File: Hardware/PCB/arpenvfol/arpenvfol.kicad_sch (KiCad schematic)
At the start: 74 parts, among them J1 Synth_power_2x5, J10 3_pin_Molex_header, J2 AudioJack2_SwitchT, J3 AudioJack2_SwitchT, J4 AudioJack2_SwitchT, J5 AudioJack2, J6 AudioJack2, J7 2_pin_Molex_connector, J8 2_pin_Molex_header, J9 3_pin_Molex_connector, Q1 2N3904, Q2 2N3904, U1 TL074

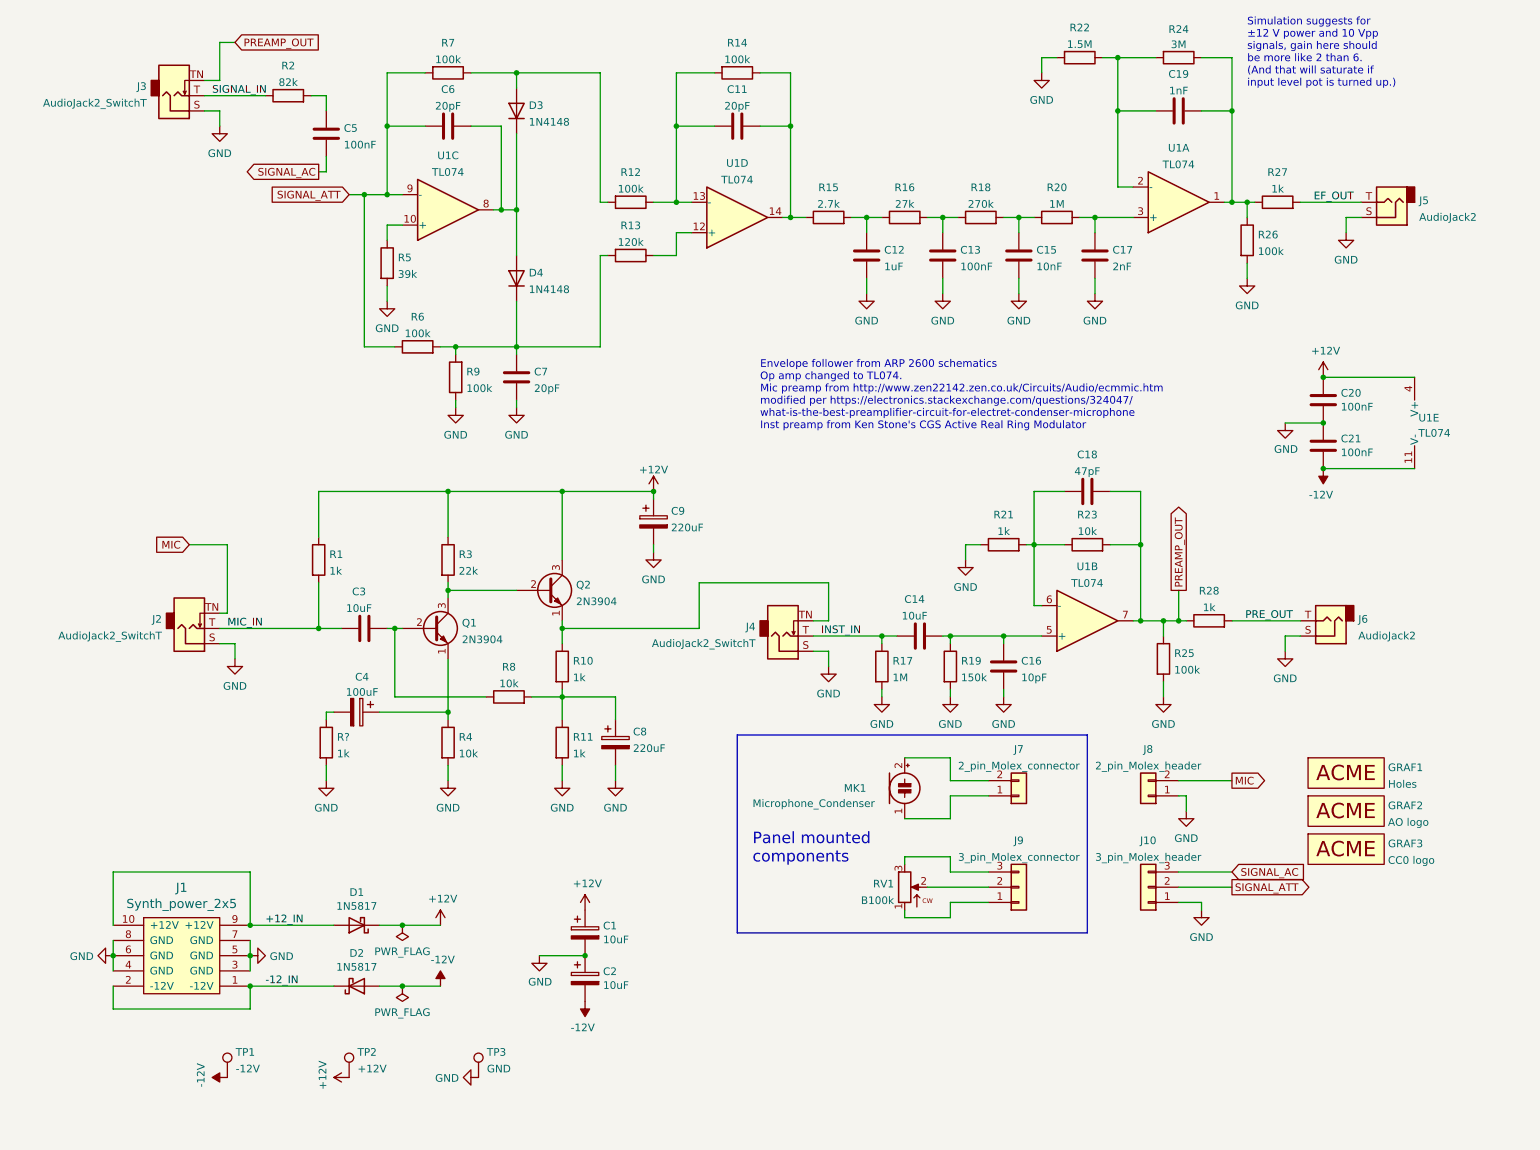
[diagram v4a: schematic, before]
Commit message: Change transistor, annotate, LTSpice simulation
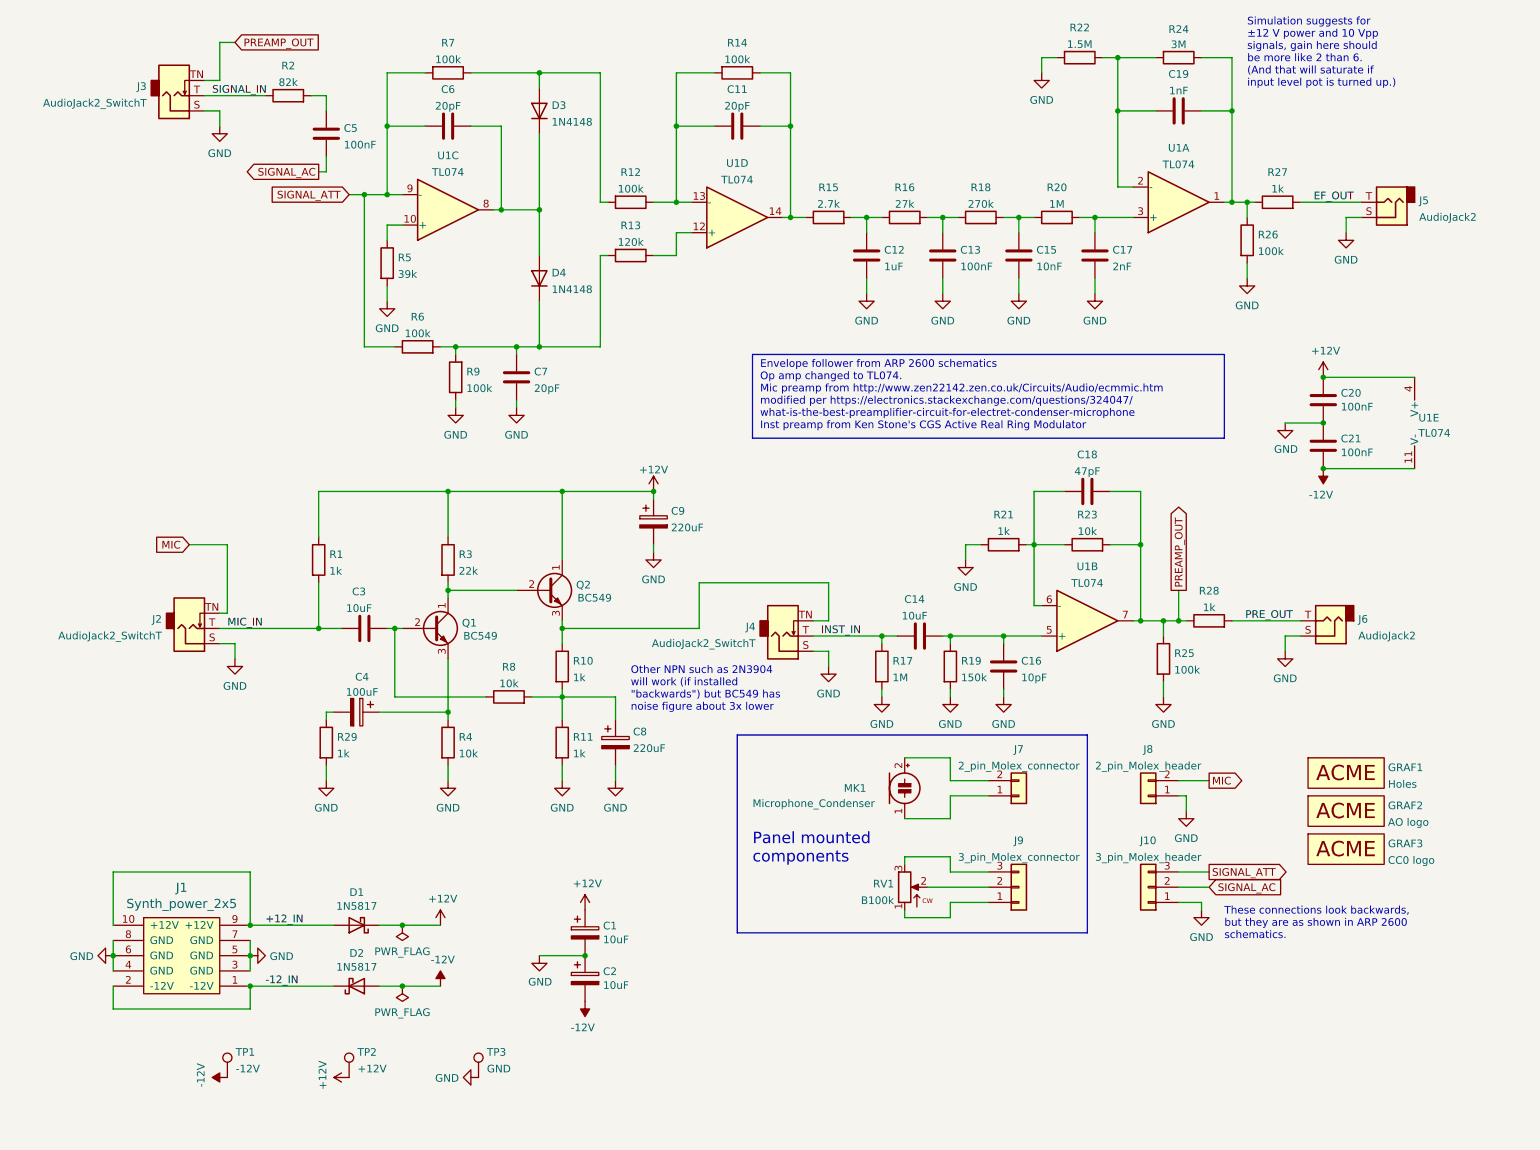
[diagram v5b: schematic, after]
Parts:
- C12: footprint ao_tht:C_Rect_L7.2mm_W2.5mm_P5.00mm_FKS2_FKP2_MKS2_MKP2 -> ao_tht:C_Rect_L7.2mm_W7.2mm_P5.00mm_FKS2_FKP2_MKS2_MKP2
- Q1, Q2: value 2N3904 -> BC549; symbol ao_symbols:2N3904 -> Transistor_BJT:BC549
- gave numbers to parts that had none: 1
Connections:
- net +12V: now also Q2.1 (C); no longer Q2.3 (C)
- net SIGNAL_AC: now also J10.2 (Pin_2); no longer J10.3 (Pin_3)
- net SIGNAL_ATT: now also J10.3 (Pin_3); no longer J10.2 (Pin_2)
- net at C4.1, R4.1: now also Q1.3 (E); no longer Q1.1 (E)
- net at Q2.2 (B), R3.2: now also Q1.1 (C); no longer Q1.3 (C)
- net at J4.TN, R10.1: now also Q2.3 (E); no longer Q2.1 (E)
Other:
- note added: "Other NPN such as 2N3904 will work (if installed "backwards") but BC549 has noise figure about 3x lower"
- note added: "These connections look backwards, but they are as shown in ARP 2600 schematics."
- moved on the sheet: D3, D4

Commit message: Panel; add gain pot
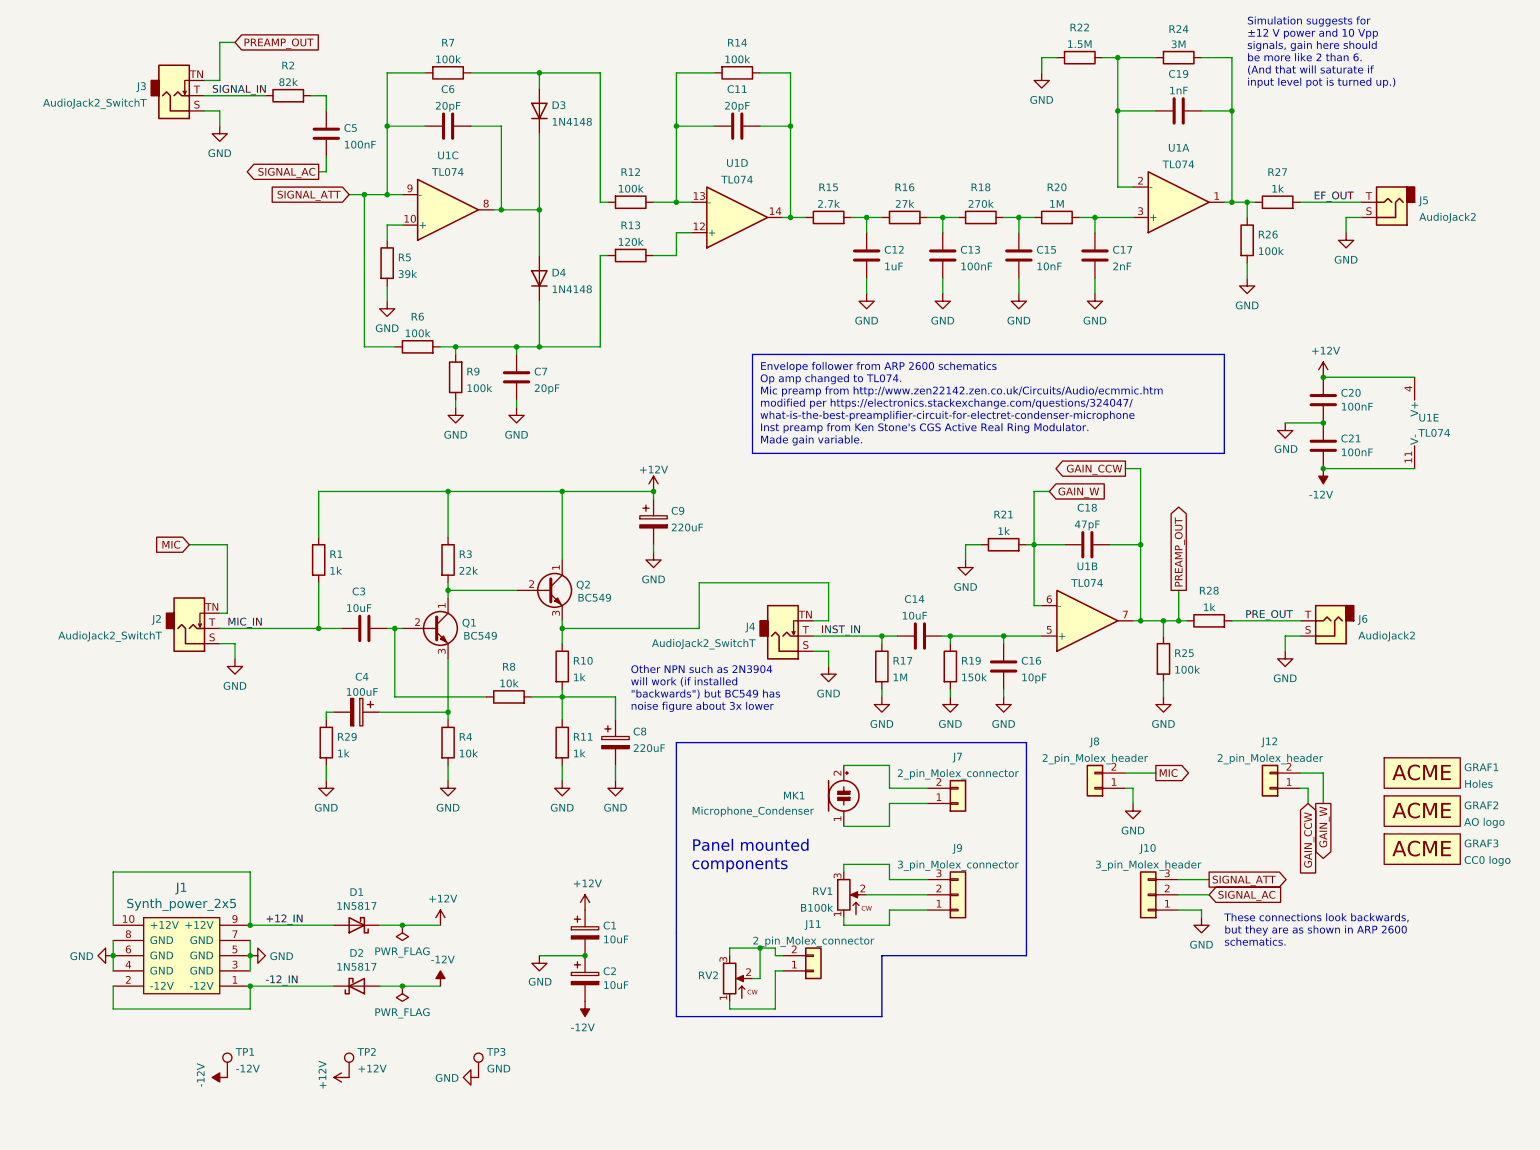
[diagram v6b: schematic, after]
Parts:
- removed R23: 10k, ao_tht:R_Axial_DIN0207_L6.3mm_D2.5mm_P10.16mm_Horizontal, symbol ao_symbols:R
- added J11: 2_pin_Molex_connector, ao_tht:Molex_KK-254_AE-6410-02A_1x02_P2.54mm_Vertical, symbol ao_symbols:2_pin_Molex_connector
- added J12: 2_pin_Molex_header, ao_tht:Molex_KK-254_AE-6410-02A_1x02_P2.54mm_Vertical, symbol ao_symbols:2_pin_Molex_header
- added RV2: (no value), symbol ao_symbols:R_POT
- C11, C16, C18, C6, C7: footprint ao_tht:C_Disc_D3.0mm_W1.6mm_P2.50mm -> (none)
- C12: footprint ao_tht:C_Rect_L7.2mm_W7.2mm_P5.00mm_FKS2_FKP2_MKS2_MKP2 -> (none)
- C13, C15, C17, C19, C5: footprint ao_tht:C_Rect_L7.2mm_W2.5mm_P5.00mm_FKS2_FKP2_MKS2_MKP2 -> (none)
- C14, C3: footprint ao_tht:C_Radial_D8.0mm_H11.5mm_P3.50mm -> (none)
- J7: footprint (none) -> ao_tht:Molex_KK-254_AE-6410-02A_1x02_P2.54mm_Vertical
- J9: footprint (none) -> ao_tht:Molex_KK-254_AE-6410-03A_1x03_P2.54mm_Vertical
- Q1, Q2: footprint ao_tht:TO-92_Inline_Wide -> (none)
- TP1, TP2: Config (none) -> DNF
- TP3: footprint ao_tht:TestPoint_THTPad_1.5x1.5mm_Drill0.7mm -> (none); Config (none) -> DNF
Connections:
- net GAIN_W: now reaches C18.1, R21.2, U1.6 (-)
- net GAIN_W: now also J12.2 (Pin_2)
- net PREAMP_OUT renamed GAIN_CCW
- net GAIN_CCW: now also J12.1 (Pin_1)
- new net: J11.1 (Pin_1), RV2.1
- new net: J11.2 (Pin_2), RV2.2, RV2.3
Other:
- note added: "Envelope follower from ARP 2600 schematics Op amp changed to TL074. Mic preamp from http://www.zen22142.zen.co.uk/Circuits/Audio/ecmmic.htm modified per https://electronics.stackexchange.com/questions/324047/ what-is-the-best-preamplifier-circuit-for-electret-condenser-microphone Inst preamp from Ken Stone's CGS Active Real Ring Modulator. Made gain variable."
- note removed: "Envelope follower from ARP 2600 schematics Op amp changed to TL074. Mic preamp from http://www.zen22142.zen.co.uk/Circuits/Audio/ecmmic.htm modified per https://electronics.stackexchange.com/questions/324047/ what-is-the-best-preamplifier-circuit-for-electret-condenser-microphone Inst preamp from Ken Stone's CGS Active Real Ring Modulator"
- moved on the sheet: C18, GRAF1, GRAF2, GRAF3, J10, J7, J8, J9, MK1, RV1

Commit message: Schem reorg
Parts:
- C11, C16, C18, C6, C7: footprint (none) -> ao_tht:C_Disc_D5.0mm_W2.5mm_P5.00mm
- C12: footprint (none) -> ao_tht:C_Rect_L7.2mm_W7.2mm_P5.00mm_FKS2_FKP2_MKS2_MKP2
- C13, C15, C17, C19, C5: footprint (none) -> ao_tht:C_Rect_L7.2mm_W2.5mm_P5.00mm_FKS2_FKP2_MKS2_MKP2
- C14, C3: footprint (none) -> ao_tht:C_Radial_D8.0mm_H11.5mm_P3.50mm
- Q1, Q2: footprint (none) -> ao_tht:TO-92_Inline_Wide
- RV2: value (none) -> B10k
- TP3: footprint (none) -> ao_tht:TestPoint_THTPad_1.5x1.5mm_Drill0.7mm
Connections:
- net MIC_OUT: now reaches J4.TN, Q2.3 (E), R10.1
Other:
- note added: "Follower"
- note added: "For ±12 V power and 10 Vpp signals, gain here should be more like 2 than 6. (And that will saturate if input level pot is turned up.)"
- note added: "Instrument preamp"
- note added: "Mic preamp"
- note added: "Power"
- note removed: "Simulation suggests for ±12 V power and 10 Vpp signals, gain here should be more like 2 than 6. (And that will saturate if input level pot is turned up.)"
- moved on the sheet: C1, C11, C12, C13, C14, C15, C16, C17, C18, C2, C20, C21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

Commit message: Final pre fab tweaks, Gerbers, schematic, BOM
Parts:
- C1: renamed from C4; value 100uF -> (none); footprint ao_tht:CP_Radial_D6.3mm_P2.50mm -> (none); SKU (none) -> A-4538
- C10: renamed from C20; value 100nF -> (none); footprint ao_tht:C_Disc_D3.0mm_W1.6mm_P2.50mm -> (none)
- C11: renamed from C21; value 100nF -> (none); footprint ao_tht:C_Disc_D3.0mm_W1.6mm_P2.50mm -> (none)
- C12: renamed from C11; value 20pF -> (none); footprint ao_tht:C_Disc_D5.0mm_W2.5mm_P5.00mm -> (none)
- C13: renamed from C12; value 1uF -> (none); footprint ao_tht:C_Rect_L7.2mm_W7.2mm_P5.00mm_FKS2_FKP2_MKS2_MKP2 -> (none); SKU (none) -> A-4168
- C14: renamed from C13; value 100nF -> (none); footprint ao_tht:C_Rect_L7.2mm_W2.5mm_P5.00mm_FKS2_FKP2_MKS2_MKP2 -> (none); SKU (none) -> A-564
- C15: renamed from C14; value 10uF -> (none); footprint ao_tht:C_Radial_D8.0mm_H11.5mm_P3.50mm -> (none); SKU A-4349 -> A-4216
- C16: renamed from C15; value 10nF -> (none); footprint ao_tht:C_Rect_L7.2mm_W2.5mm_P5.00mm_FKS2_FKP2_MKS2_MKP2 -> (none); SKU (none) -> A-559
- C17: renamed from C16; value 10pF -> (none); footprint ao_tht:C_Disc_D5.0mm_W2.5mm_P5.00mm -> (none)
- C18: renamed from C17; value 2nF -> (none); footprint ao_tht:C_Rect_L7.2mm_W2.5mm_P5.00mm_FKS2_FKP2_MKS2_MKP2 -> (none); SKU (none) -> A-558
- C19: renamed from C18; value 47pF -> (none); footprint ao_tht:C_Disc_D5.0mm_W2.5mm_P5.00mm -> (none)
- C2: renamed from C5; value 100nF -> (none); footprint ao_tht:C_Rect_L7.2mm_W2.5mm_P5.00mm_FKS2_FKP2_MKS2_MKP2 -> (none); SKU (none) -> A-564
- C20: renamed from C19; value 1nF -> (none); footprint ao_tht:C_Rect_L7.2mm_W2.5mm_P5.00mm_FKS2_FKP2_MKS2_MKP2 -> (none); SKU (none) -> A-1531, A-557
- C3: value 10uF -> (none); footprint ao_tht:C_Radial_D8.0mm_H11.5mm_P3.50mm -> (none); SKU A-4349 -> A-4216
- C4: renamed from C6; value 20pF -> (none); footprint ao_tht:C_Disc_D5.0mm_W2.5mm_P5.00mm -> (none)
- C5: renamed from C7; value 20pF -> (none); footprint ao_tht:C_Disc_D5.0mm_W2.5mm_P5.00mm -> (none)
- C6: renamed from C1; value 10uF -> (none); footprint ao_tht:CP_Radial_D6.3mm_P2.50mm -> (none)
- C7: renamed from C2; value 10uF -> (none); footprint ao_tht:CP_Radial_D6.3mm_P2.50mm -> (none)
- C8, C9: value 220uF -> (none); footprint ao_tht:CP_Radial_D6.3mm_P2.50mm -> (none); SKU (none) -> A-1064
- D1, D2: value 1N5817 -> (none); footprint ao_tht:D_DO-41_SOD81_P10.16mm_Horizontal -> (none)
- D3, D4: value 1N4148 -> (none); footprint ao_tht:D_DO-35_SOD27_P7.62mm_Horizontal -> (none)
- GRAF1: value Holes -> (none); footprint arpenvfol:arpenvfol_panel_holes -> (none)
- GRAF2: value AO logo -> (none); footprint ao_tht:analogoutput_12mm -> (none)
- GRAF3: value CC0 logo -> (none); footprint ao_tht:CC0_logo -> (none)
- J1: renamed from J2; value AudioJack2_SwitchT -> (none); footprint ao_tht:Jack_6.35mm_PJ_629HAN_slots -> (none)
- J10: value 3_pin_Molex_header -> (none); footprint ao_tht:Molex_KK-254_AE-6410-03A_1x03_P2.54mm_Vertical -> (none)
- J11: renamed from J5; value AudioJack2 -> (none); footprint ao_tht:Jack_6.35mm_PJ_629HAN_slots -> (none)
- J12: renamed from J6; value AudioJack2 -> (none); footprint ao_tht:Jack_6.35mm_PJ_629HAN_slots -> (none)
- J2: renamed from J3; value AudioJack2_SwitchT -> (none); footprint ao_tht:Jack_6.35mm_PJ_629HAN_slots -> (none)
- J3: renamed from J1; value Synth_power_2x5 -> (none); footprint ao_tht:Power_Header -> (none)
- J4: value AudioJack2_SwitchT -> (none); footprint ao_tht:Jack_6.35mm_PJ_629HAN_slots -> (none)
- J5: renamed from J7; value 2_pin_Molex_connector -> (none); footprint ao_tht:Molex_KK-254_AE-6410-02A_1x02_P2.54mm_Vertical -> (none)
- J6: renamed from J11; value 2_pin_Molex_connector -> (none); footprint ao_tht:Molex_KK-254_AE-6410-02A_1x02_P2.54mm_Vertical -> (none)
- J7: renamed from J9; value 3_pin_Molex_connector -> (none); footprint ao_tht:Molex_KK-254_AE-6410-03A_1x03_P2.54mm_Vertical -> (none)
- J8: value 2_pin_Molex_header -> (none); footprint ao_tht:Molex_KK-254_AE-6410-02A_1x02_P2.54mm_Vertical -> (none)
- J9: renamed from J12; value 2_pin_Molex_header -> (none); footprint ao_tht:Molex_KK-254_AE-6410-02A_1x02_P2.54mm_Vertical -> (none)
- MK1: value Microphone_Condenser -> (none)
- Q1, Q2: value BC549 -> (none); footprint ao_tht:TO-92_Inline_Wide -> (none)
- R1, R27, R28: value 1k -> (none); footprint ao_tht:R_Axial_DIN0207_L6.3mm_D2.5mm_P10.16mm_Horizontal -> (none)
- R10: renamed from R8; value 10k -> (none); footprint ao_tht:R_Axial_DIN0207_L6.3mm_D2.5mm_P10.16mm_Horizontal -> (none)
- R11: renamed from R10; value 1k -> (none); footprint ao_tht:R_Axial_DIN0207_L6.3mm_D2.5mm_P10.16mm_Horizontal -> (none)
- R12: renamed from R11; value 1k -> (none); footprint ao_tht:R_Axial_DIN0207_L6.3mm_D2.5mm_P10.16mm_Horizontal -> (none)
- R13: renamed from R12; value 100k -> (none); footprint ao_tht:R_Axial_DIN0207_L6.3mm_D2.5mm_P10.16mm_Horizontal -> (none)
- R14: renamed from R13; value 120k -> (none); footprint ao_tht:R_Axial_DIN0207_L6.3mm_D2.5mm_P10.16mm_Horizontal -> (none)
- R15: renamed from R14; value 100k -> (none); footprint ao_tht:R_Axial_DIN0207_L6.3mm_D2.5mm_P10.16mm_Horizontal -> (none)
- R16: renamed from R15; value 2.7k -> (none); footprint ao_tht:R_Axial_DIN0207_L6.3mm_D2.5mm_P10.16mm_Horizontal -> (none)
- R17: renamed from R16; value 27k -> (none); footprint ao_tht:R_Axial_DIN0207_L6.3mm_D2.5mm_P10.16mm_Horizontal -> (none)
- R18: renamed from R17; value 1M -> (none); footprint ao_tht:R_Axial_DIN0207_L6.3mm_D2.5mm_P10.16mm_Horizontal -> (none)
- R19: renamed from R18; value 270k -> (none); footprint ao_tht:R_Axial_DIN0207_L6.3mm_D2.5mm_P10.16mm_Horizontal -> (none)
- R2: value 82k -> (none); footprint ao_tht:R_Axial_DIN0207_L6.3mm_D2.5mm_P10.16mm_Horizontal -> (none)
- R20: renamed from R19; value 150k -> (none); footprint ao_tht:R_Axial_DIN0207_L6.3mm_D2.5mm_P10.16mm_Horizontal -> (none)
- R21: renamed from R20; value 1M -> (none); footprint ao_tht:R_Axial_DIN0207_L6.3mm_D2.5mm_P10.16mm_Horizontal -> (none)
- R22: value 1.5M -> (none); footprint ao_tht:R_Axial_DIN0207_L6.3mm_D2.5mm_P10.16mm_Horizontal -> (none)
- R23: renamed from R21; value 1k -> (none); footprint ao_tht:R_Axial_DIN0207_L6.3mm_D2.5mm_P10.16mm_Horizontal -> (none)
- R24: value 3M -> (none); footprint ao_tht:R_Axial_DIN0207_L6.3mm_D2.5mm_P10.16mm_Horizontal -> (none)
- R25: renamed from R26; value 100k -> (none); footprint ao_tht:R_Axial_DIN0207_L6.3mm_D2.5mm_P10.16mm_Horizontal -> (none)
- R26: renamed from R25; value 100k -> (none); footprint ao_tht:R_Axial_DIN0207_L6.3mm_D2.5mm_P10.16mm_Horizontal -> (none)
- R3: renamed from R29; value 1k -> (none); footprint ao_tht:R_Axial_DIN0207_L6.3mm_D2.5mm_P10.16mm_Horizontal -> (none)
- R4: renamed from R5; value 39k -> (none); footprint ao_tht:R_Axial_DIN0207_L6.3mm_D2.5mm_P10.16mm_Horizontal -> (none)
- R5: renamed from R3; value 22k -> (none); footprint ao_tht:R_Axial_DIN0207_L6.3mm_D2.5mm_P10.16mm_Horizontal -> (none)
- R6: renamed from R4; value 10k -> (none); footprint ao_tht:R_Axial_DIN0207_L6.3mm_D2.5mm_P10.16mm_Horizontal -> (none)
- R7: renamed from R6; value 100k -> (none); footprint ao_tht:R_Axial_DIN0207_L6.3mm_D2.5mm_P10.16mm_Horizontal -> (none)
- R8: renamed from R7; value 100k -> (none); footprint ao_tht:R_Axial_DIN0207_L6.3mm_D2.5mm_P10.16mm_Horizontal -> (none)
- R9: value 100k -> (none); footprint ao_tht:R_Axial_DIN0207_L6.3mm_D2.5mm_P10.16mm_Horizontal -> (none)
- RV1: renamed from RV2; value B10k -> (none)
- RV2: renamed from RV1; value B100k -> (none)
- TP1: value -12V -> (none); footprint ao_tht:TestPoint_THTPad_D1.5mm_Drill0.7mm -> (none)
- TP2: value +12V -> (none); footprint ao_tht:TestPoint_THTPad_D1.5mm_Drill0.7mm -> (none)
- TP3: value GND -> (none); footprint ao_tht:TestPoint_THTPad_1.5x1.5mm_Drill0.7mm -> (none)
- U1: value TL074 -> (none); footprint ao_tht:DIP-14_W7.62mm_Socket_LongPads -> (none)
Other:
- note added: "Partly due to ±12 V power, breadboard tests seemed to indicate gain here should be more like 2 than 6. (And that will saturate if input level pot is turned up.)"
- note removed: "For ±12 V power and 10 Vpp signals, gain here should be more like 2 than 6. (And that will saturate if input level pot is turned up.)"
